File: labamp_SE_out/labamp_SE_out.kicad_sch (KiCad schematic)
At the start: 22 parts, among them J1 Conn_02x06_Odd_Even, J2 Conn_02x06_Odd_Even, J3 Conn_01x03, U1 ${SIM.PARAMS}

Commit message: Added resistors to unused out- net to gnd
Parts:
- added R6: R, Resistor_SMD:R_0603_1608Metric_Pad0.98x0.95mm_HandSolder, symbol Device:R
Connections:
- net GND: now also R6.1; no longer J2.10 (Pin_10)
- new net out-: J2.10 (Pin_10), R6.2
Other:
- moved on the sheet: R5
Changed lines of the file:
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@@
 	(wire
 		(pts
-			(xy 244.475 99.06) (xy 232.41 99.06)
+			(xy 244.475 99.06) (xy 224.79 99.06)
 		)
 		(stroke
@@
 	(wire
 		(pts
-			(xy 172.72 91.44) (xy 198.12 91.44)
+			(xy 172.72 91.44) (xy 217.17 91.44)
 		)
 		(stroke
@@
 	(wire
 		(pts
-			(xy 205.74 91.44) (xy 244.475 91.44)
+			(xy 224.79 91.44) (xy 244.475 91.44)
 		)
 		(stroke
@@
 	(wire
 		(pts
+			(xy 217.17 99.06) (xy 210.82 99.06)
+		)
+		(stroke
+			(width 0)
+			(type default)
+		)
+	)
+	(wire
+		(pts
 			(xy 166.37 128.27) (xy 172.72 128.27)
 		)
@@
 	(wire
 		(pts
-			(xy 232.41 99.06) (xy 232.41 104.14)
+			(xy 210.82 99.06) (xy 210.82 104.14)
 		)
 		(stroke
@@
 	(symbol
 		(lib_id "Device:R")
-		(at 201.93 91.44 90)
+		(at 220.98 91.44 90)
 		(unit 1)
 		(exclude_from_sim no)
@@
 		(dnp no)
 		(property "Reference" "R5"
-			(at 201.93 87.122 90)
+			(at 220.98 87.122 90)
 			(effects
 				(font
@@
 		)
 		(property "Value" "R"
-			(at 201.93 89.154 90)
+			(at 220.98 89.154 90)
 			(effects
 				(font
@@
 		)
 		(property "Footprint" "Resistor_SMD:R_0603_1608Metric_Pad0.98x0.95mm_HandSolder"
-			(at 201.93 93.218 90)
+			(at 220.98 93.218 90)
 			(effects
 				(font
@@
 		)
 		(property "Datasheet" "~"
-			(at 201.93 91.44 0)
+			(at 220.98 91.44 0)
 			(effects
 				(font
@@
 		)
 		(property "Description" "Resistor"
-			(at 201.93 91.44 0)
+			(at 220.98 91.44 0)
 			(effects
 				(font
@@
 	)
 	(symbol
+		(lib_id "Device:R")
+		(at 220.98 99.06 90)
+		(unit 1)
+		(exclude_from_sim no)
+		(in_bom yes)
+		(on_board yes)
+		(dnp no)
+		(property "Reference" "R6"
+			(at 220.98 94.742 90)
+			(effects
+				(font
+					(size 1.27 1.27)
+				)
+			)
+		)
+		(property "Value" "R"
+			(at 220.98 96.774 90)
+			(effects
+				(font
+					(size 1.27 1.27)
+				)
+			)
+		)
+		(property "Footprint" "Resistor_SMD:R_0603_1608Metric_Pad0.98x0.95mm_HandSolder"
+			(at 220.98 100.838 90)
+			(effects
+				(font
+					(size 1.27 1.27)
+				)
+				(hide yes)
+			)
+		)
+		(property "Datasheet" "~"
+			(at 220.98 99.06 0)
+			(effects
+				(font
+					(size 1.27 1.27)
+				)
+				(hide yes)
+			)
+		)
+		(property "Description" "Resistor"
+			(at 220.98 99.06 0)
+			(effects
+				(font
+					(size 1.27 1.27)
+				)
+				(hide yes)
+			)
+		)
+		(pin "2"
+		)
+		(pin "1"
+		)
+		(instances
+			(project "labamp_SE_out"
+				(path "/a0c99055-08c7-4e05-9803-96c7ce32a2b2"
+					(reference "R6")
+					(unit 1)
+				)
+			)
+		)
+	)
+	(symbol
 		(lib_id "power:GND")
 		(at 54.61 104.14 0)
@@
 	(symbol
 		(lib_id "power:GND")
-		(at 232.41 104.14 0)
+		(at 210.82 104.14 0)
 		(mirror y)
 		(unit 1)
@@
 		(fields_autoplaced yes)
 		(property "Reference" "#PWR031"
-			(at 232.41 110.49 0)
+			(at 210.82 110.49 0)
 			(effects
 				(font
@@
 		)
 		(property "Value" "GND"
-			(at 232.41 109.22 0)
+			(at 210.82 109.22 0)
 			(effects
 				(font
@@
 		)
 		(property "Footprint" ""
-			(at 232.41 104.14 0)
+			(at 210.82 104.14 0)
 			(effects
 				(font
@@
 		)
 		(property "Datasheet" ""
-			(at 232.41 104.14 0)
+			(at 210.82 104.14 0)
 			(effects
 				(font
@@
 		)
 		(property "Description" "Power symbol creates a global label with name \"GND\" , ground"
-			(at 232.41 104.14 0)
+			(at 210.82 104.14 0)
 			(effects
 				(font

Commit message: Routed Single ended output PCB
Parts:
- removed R4: R, Resistor_SMD:R_0603_1608Metric_Pad0.98x0.95mm_HandSolder, symbol Device:R
- added R3, R5: R, Resistor_SMD:R_0603_1608Metric_Pad0.98x0.95mm_HandSolder, symbol Device:R
- renumbered R3 to R4, R5 to R7
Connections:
- net GND: now also R5.2
- net in-: now also R3.1; no longer C9.1, R4.1, U1.2 (-)
- new net: C9.1, R3.2, R4.1, R5.1, U1.2 (-)
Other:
- moved on the sheet: R1
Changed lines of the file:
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@@
+	)
+	(junction
+		(at 240.665 96.52)
+		(diameter 0)
+		(color 0 0 0 0)
+	)
+	(junction
+		(at 240.665 93.98)
+		(diameter 0)
+		(color 0 0 0 0)
+	)
+	(junction
+		(at 260.985 101.6)
+		(diameter 0)
+		(color 0 0 0 0)
+	)
+	(junction
+		(at 260.985 93.98)
+		(diameter 0)
+		(color 0 0 0 0)
+	)
+	(junction
+		(at 134.62 91.44)
+		(diameter 0)
+		(color 0 0 0 0)
+	)
+	(junction
+		(at 34.29 101.6)
+		(diameter 0)
+		(color 0 0 0 0)
+	)
+	(junction
+		(at 54.61 101.6)
+		(diameter 0)
+		(color 0 0 0 0)
+	)
+	(junction
+		(at 50.8 176.53)
+		(diameter 0)
+		(color 0 0 0 0)
 	)
 	(junction
@@
 	)
 	(junction
-		(at 240.665 96.52)
-		(diameter 0)
-		(color 0 0 0 0)
-	)
-	(junction
-		(at 240.665 93.98)
-		(diameter 0)
-		(color 0 0 0 0)
-	)
-	(junction
-		(at 260.985 101.6)
-		(diameter 0)
-		(color 0 0 0 0)
-	)
-	(junction
-		(at 260.985 93.98)
-		(diameter 0)
-		(color 0 0 0 0)
-	)
-	(junction
-		(at 134.62 91.44)
-		(diameter 0)
-		(color 0 0 0 0)
-	)
-	(junction
-		(at 34.29 101.6)
-		(diameter 0)
-		(color 0 0 0 0)
-	)
-	(junction
-		(at 54.61 101.6)
-		(diameter 0)
-		(color 0 0 0 0)
-	)
-	(junction
-		(at 50.8 176.53)
-		(diameter 0)
-		(color 0 0 0 0)
-	)
-	(junction
 		(at 147.32 118.11)
 		(diameter 0)
@@
 	(wire
 		(pts
-			(xy 147.32 99.06) (xy 50.8 99.06)
+			(xy 147.32 99.06) (xy 113.03 99.06)
 		)
 		(stroke
@@
 	(wire
 		(pts
+			(xy 147.32 139.7) (xy 147.32 143.51)
+		)
+		(stroke
+			(width 0)
+			(type default)
+		)
+	)
+	(wire
+		(pts
 			(xy 34.29 124.46) (xy 34.29 127)
 		)
@@
 	(wire
 		(pts
+			(xy 147.32 128.27) (xy 147.32 132.08)
+		)
+		(stroke
+			(width 0)
+			(type default)
+		)
+	)
+	(wire
+		(pts
 			(xy 50.8 101.6) (xy 54.61 101.6)
 		)
@@
 	(wire
 		(pts
-			(xy 50.8 91.44) (xy 116.84 91.44)
+			(xy 50.8 91.44) (xy 105.41 91.44)
 		)
 		(stroke
@@
 	(wire
 		(pts
-			(xy 124.46 91.44) (xy 134.62 91.44)
+			(xy 113.03 91.44) (xy 134.62 91.44)
 		)
 		(stroke
@@
 	(wire
 		(pts
-			(xy 147.32 128.27) (xy 147.32 130.81)
-		)
-		(stroke
-			(width 0)
-			(type default)
-		)
-	)
-	(wire
-		(pts
 			(xy 147.32 99.06) (xy 147.32 118.11)
 		)
@@
 	(wire
 		(pts
-			(xy 147.32 138.43) (xy 147.32 143.51)
+			(xy 105.41 99.06) (xy 50.8 99.06)
 		)
 		(stroke
@@
 	(symbol
 		(lib_id "Device:R")
+		(at 147.32 135.89 0)
+		(unit 1)
+		(exclude_from_sim no)
+		(in_bom yes)
+		(on_board yes)
+		(dnp no)
+		(fields_autoplaced yes)
+		(property "Reference" "R5"
+			(at 149.86 134.6199 0)
+			(effects
+				(font
+					(size 1.27 1.27)
+				)
+				(justify left)
+			)
+		)
+		(property "Value" "R"
+			(at 149.86 137.1599 0)
+			(effects
+				(font
+					(size 1.27 1.27)
+				)
+				(justify left)
+			)
+		)
+		(property "Footprint" "Resistor_SMD:R_0603_1608Metric_Pad0.98x0.95mm_HandSolder"
+			(at 145.542 135.89 90)
+			(effects
+				(font
+					(size 1.27 1.27)
+				)
+				(hide yes)
+			)
+		)
+		(property "Datasheet" "~"
+			(at 147.32 135.89 0)
+			(effects
+				(font
+					(size 1.27 1.27)
+				)
+				(hide yes)
+			)
+		)
+		(property "Description" "Resistor"
+			(at 147.32 135.89 0)
+			(effects
+				(font
+					(size 1.27 1.27)
+				)
+				(hide yes)
+			)
+		)
+		(pin "2"
+		)
+		(pin "1"
+		)
+		(instances
+			(project "labamp_SE_out"
+				(path "/a0c99055-08c7-4e05-9803-96c7ce32a2b2"
+					(reference "R5")
+					(unit 1)
+				)
+			)
+		)
+	)
+	(symbol
+		(lib_id "Device:R")
 		(at 162.56 118.11 90)
 		(unit 1)
@@
 		(on_board yes)
 		(dnp no)
-		(property "Reference" "R3"
+		(property "Reference" "R4"
 			(at 162.56 113.792 90)
 			(effects
@@
 			(project "labamp_SE_out"
 				(path "/a0c99055-08c7-4e05-9803-96c7ce32a2b2"
-					(reference "R3")
+					(reference "R4")
 					(unit 1)
 				)
@@
 	(symbol
 		(lib_id "Device:R")
-		(at 120.65 91.44 90)
+		(at 109.22 91.44 90)
 		(unit 1)
 		(exclude_from_sim no)
@@
 		(dnp no)
 		(property "Reference" "R1"
-			(at 120.65 87.122 90)
+			(at 109.22 87.122 90)
 			(effects
 				(font
@@
 		)
 		(property "Value" "R"
-			(at 120.65 89.154 90)
+			(at 109.22 89.154 90)
 			(effects
 				(font
@@
 		)
 		(property "Footprint" "Resistor_SMD:R_0603_1608Metric_Pad0.98x0.95mm_HandSolder"
-			(at 120.65 93.218 90)
+			(at 109.22 93.218 90)
 			(effects
 				(font
@@
 		)
 		(property "Datasheet" "~"
-			(at 120.65 91.44 0)
+			(at 109.22 91.44 0)
 			(effects
 				(font
@@
 		)
 		(property "Description" "Resistor"
-			(at 120.65 91.44 0)
+			(at 109.22 91.44 0)
 			(effects
 				(font
@@
 	)
 	(symbol
+		(lib_id "Device:R")
+		(at 109.22 99.06 90)
+		(unit 1)
+		(exclude_from_sim no)
+		(in_bom yes)
+		(on_board yes)
+		(dnp no)
+		(property "Reference" "R3"
+			(at 109.22 94.742 90)
+			(effects
+				(font
+					(size 1.27 1.27)
+				)
+			)
+		)
+		(property "Value" "R"
+			(at 109.22 96.774 90)
+			(effects
+				(font
+					(size 1.27 1.27)
+				)
+			)
+		)
+		(property "Footprint" "Resistor_SMD:R_0603_1608Metric_Pad0.98x0.95mm_HandSolder"
+			(at 109.22 100.838 90)
+			(effects
+				(font
+					(size 1.27 1.27)
+				)
+				(hide yes)
+			)
+		)
+		(property "Datasheet" "~"
+			(at 109.22 99.06 0)
+			(effects
+				(font
+					(size 1.27 1.27)
+				)
+				(hide yes)
+			)
+		)
+		(property "Description" "Resistor"
+			(at 109.22 99.06 0)
+			(effects
+				(font
+					(size 1.27 1.27)
+				)
+				(hide yes)
+			)
+		)
+		(pin "2"
+		)
+		(pin "1"
+		)
+		(instances
+			(project "labamp_SE_out"
+				(path "/a0c99055-08c7-4e05-9803-96c7ce32a2b2"
+					(reference "R3")
+					(unit 1)
+				)
+			)
+		)
+	)
+	(symbol
 		(lib_id "Device:C")
 		(at 127 31.75 0)
@@
 				(path "/a0c99055-08c7-4e05-9803-96c7ce32a2b2"
 					(reference "C5")
-					(unit 1)
-				)
-			)
-		)
-	)
-	(symbol
-		(lib_id "Device:R")
-		(at 147.32 134.62 0)
-		(unit 1)
-		(exclude_from_sim no)
-		(in_bom yes)
-		(on_board yes)
-		(dnp no)
-		(property "Reference" "R4"
-			(at 149.86 133.3499 0)
-			(effects
-				(font
-					(size 1.27 1.27)
-				)
-				(justify left)
-			)
-		)
-		(property "Value" "R"
-			(at 149.86 135.8899 0)
-			(effects
-				(font
-					(size 1.27 1.27)
-				)
-				(justify left)
-			)
-		)
-		(property "Footprint" "Resistor_SMD:R_0603_1608Metric_Pad0.98x0.95mm_HandSolder"
-			(at 145.542 134.62 90)
-			(effects
-				(font
-					(size 1.27 1.27)
-				)
-				(hide yes)
-			)
-		)
-		(property "Datasheet" "~"
-			(at 147.32 134.62 0)
-			(effects
-				(font
-					(size 1.27 1.27)
-				)
-				(hide yes)
-			)
-		)
-		(property "Description" "Resistor"
-			(at 147.32 134.62 0)
-			(effects
-				(font
-					(size 1.27 1.27)
-				)
-				(hide yes)
-			)
-		)
-		(pin "2"
-		)
-		(pin "1"
-		)
-		(instances
-			(project "labamp_SE_out"
-				(path "/a0c99055-08c7-4e05-9803-96c7ce32a2b2"
-					(reference "R4")
 					(unit 1)
 				)
@@
 		(on_board yes)
 		(dnp no)
-		(property "Reference" "R5"
+		(property "Reference" "R7"
 			(at 220.98 87.122 90)
 			(effects
@@
 			(project "labamp_SE_out"
 				(path "/a0c99055-08c7-4e05-9803-96c7ce32a2b2"
-					(reference "R5")
+					(reference "R7")
 					(unit 1)
 				)

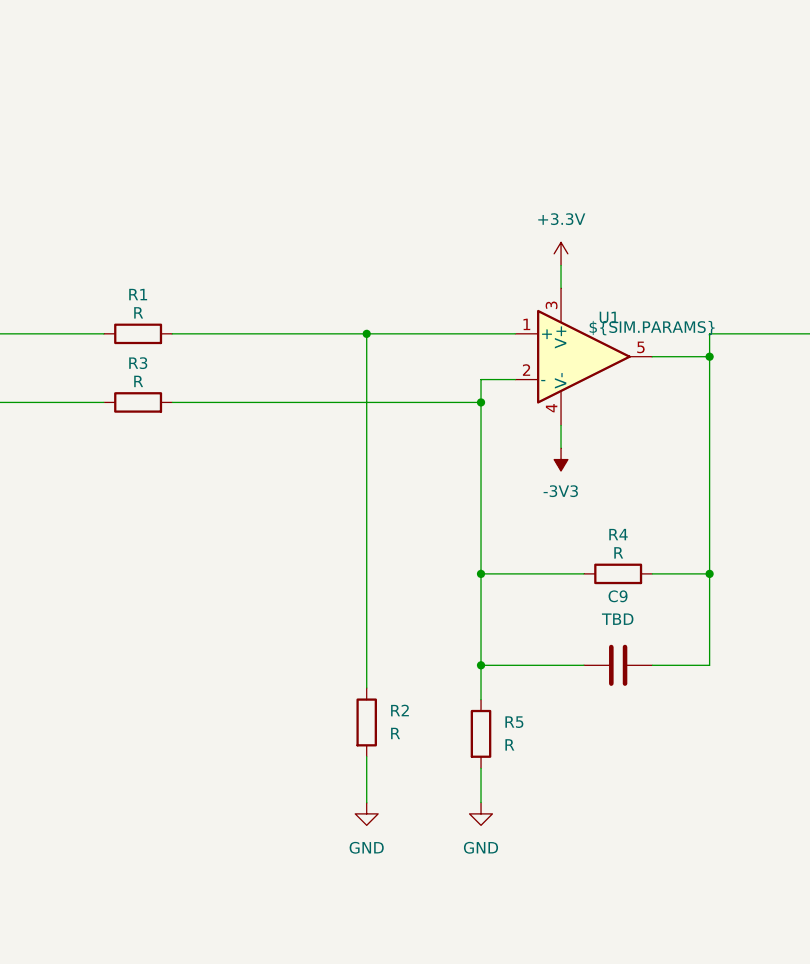
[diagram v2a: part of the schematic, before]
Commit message: Finished routing SE_out
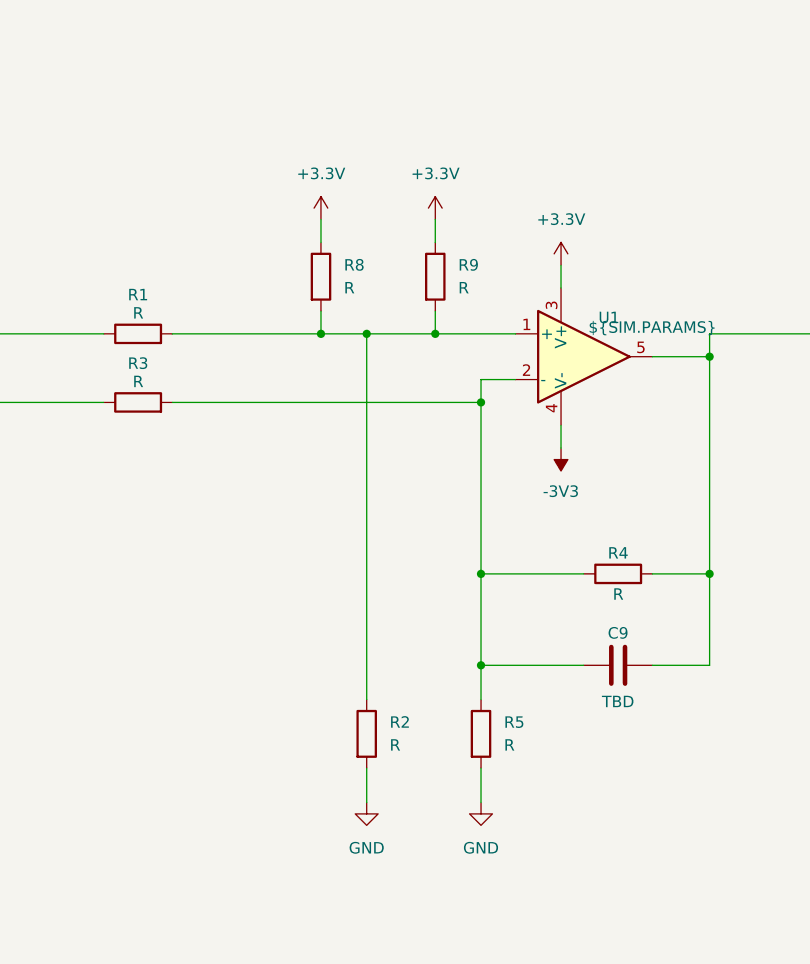
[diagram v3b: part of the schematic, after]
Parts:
- added R8, R9: R, Resistor_SMD:R_0603_1608Metric_Pad0.98x0.95mm_HandSolder, symbol Device:R
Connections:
- net +3.3V: now also R8.1, R9.1
- net at R1.2, R2.1, U1.1 (+): now also R8.2, R9.2
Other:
- moved on the sheet: R2
